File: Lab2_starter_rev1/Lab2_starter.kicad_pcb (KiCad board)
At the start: 4 copper layers, 139.7 x 101.6 mm, 77 parts, among them J1 973582101, J10 Conn_01x02, J11 Conn_01x02, J12 Conn_01x02, J13 Conn_01x02, J14 Conn_01x02, J15 Conn_01x02, J16 Conn_01x02, J2 973582100, J3 973582101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

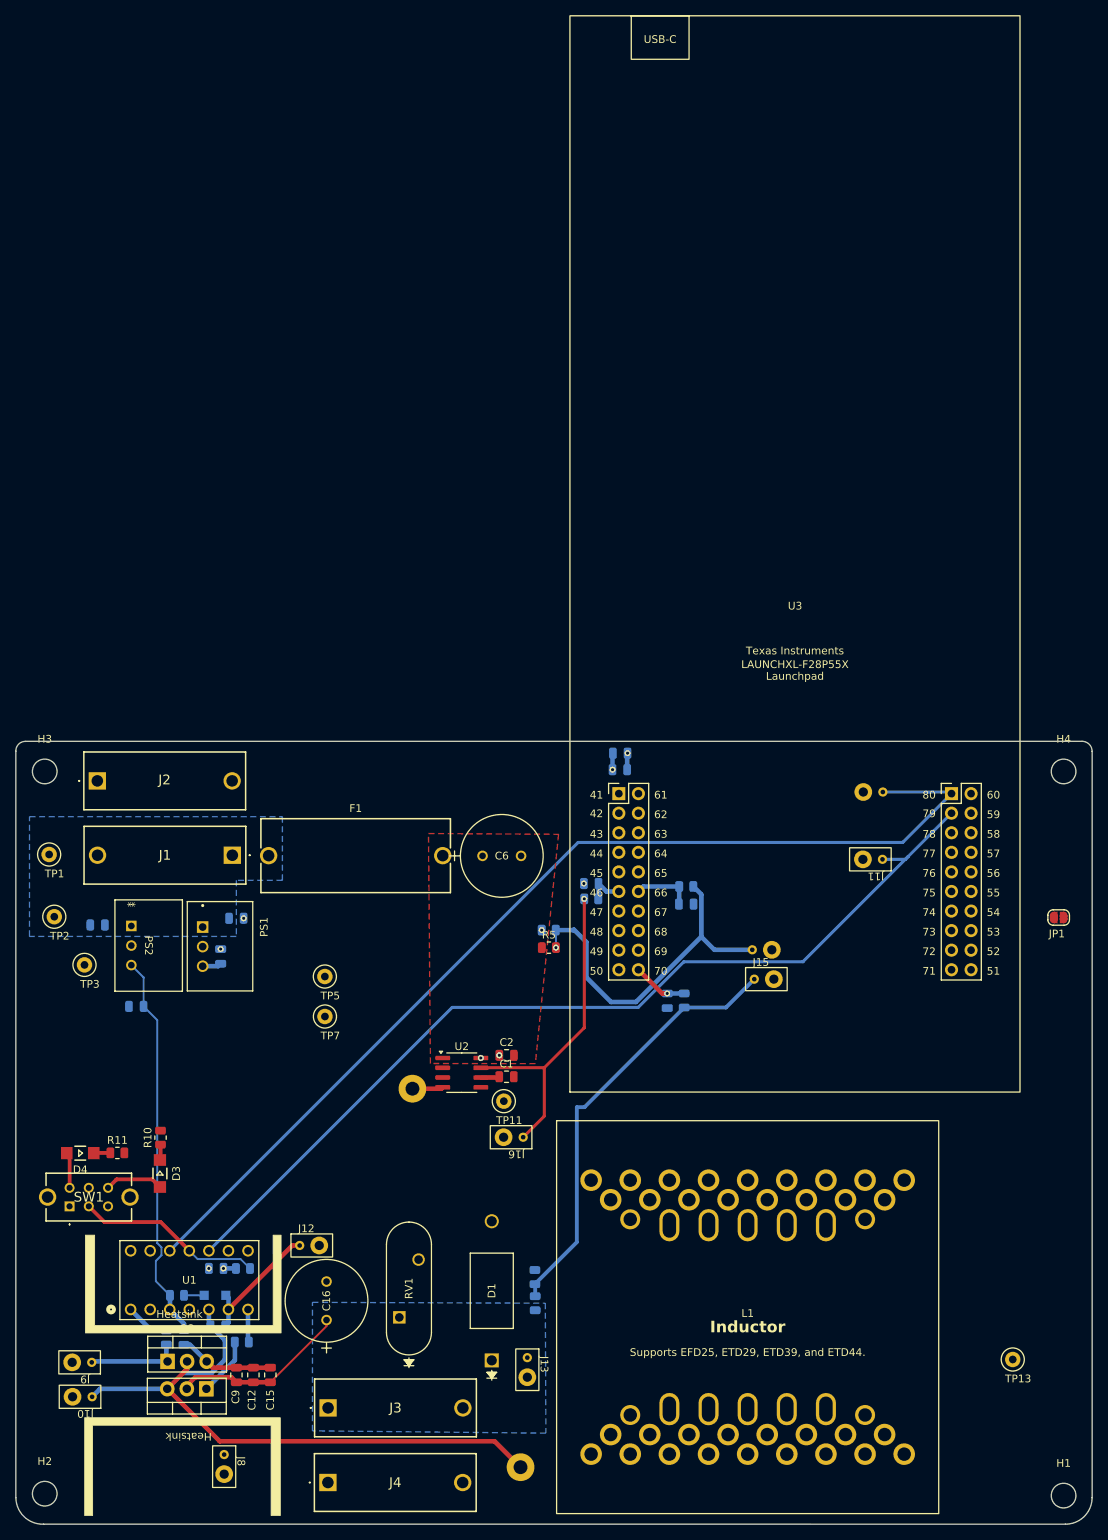
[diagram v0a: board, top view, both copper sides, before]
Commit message: Updated for first PCB upload
Added missing vias to some grounds
Increased width of a few wires
Moved many silkscreens
Added keepout zone for inductor
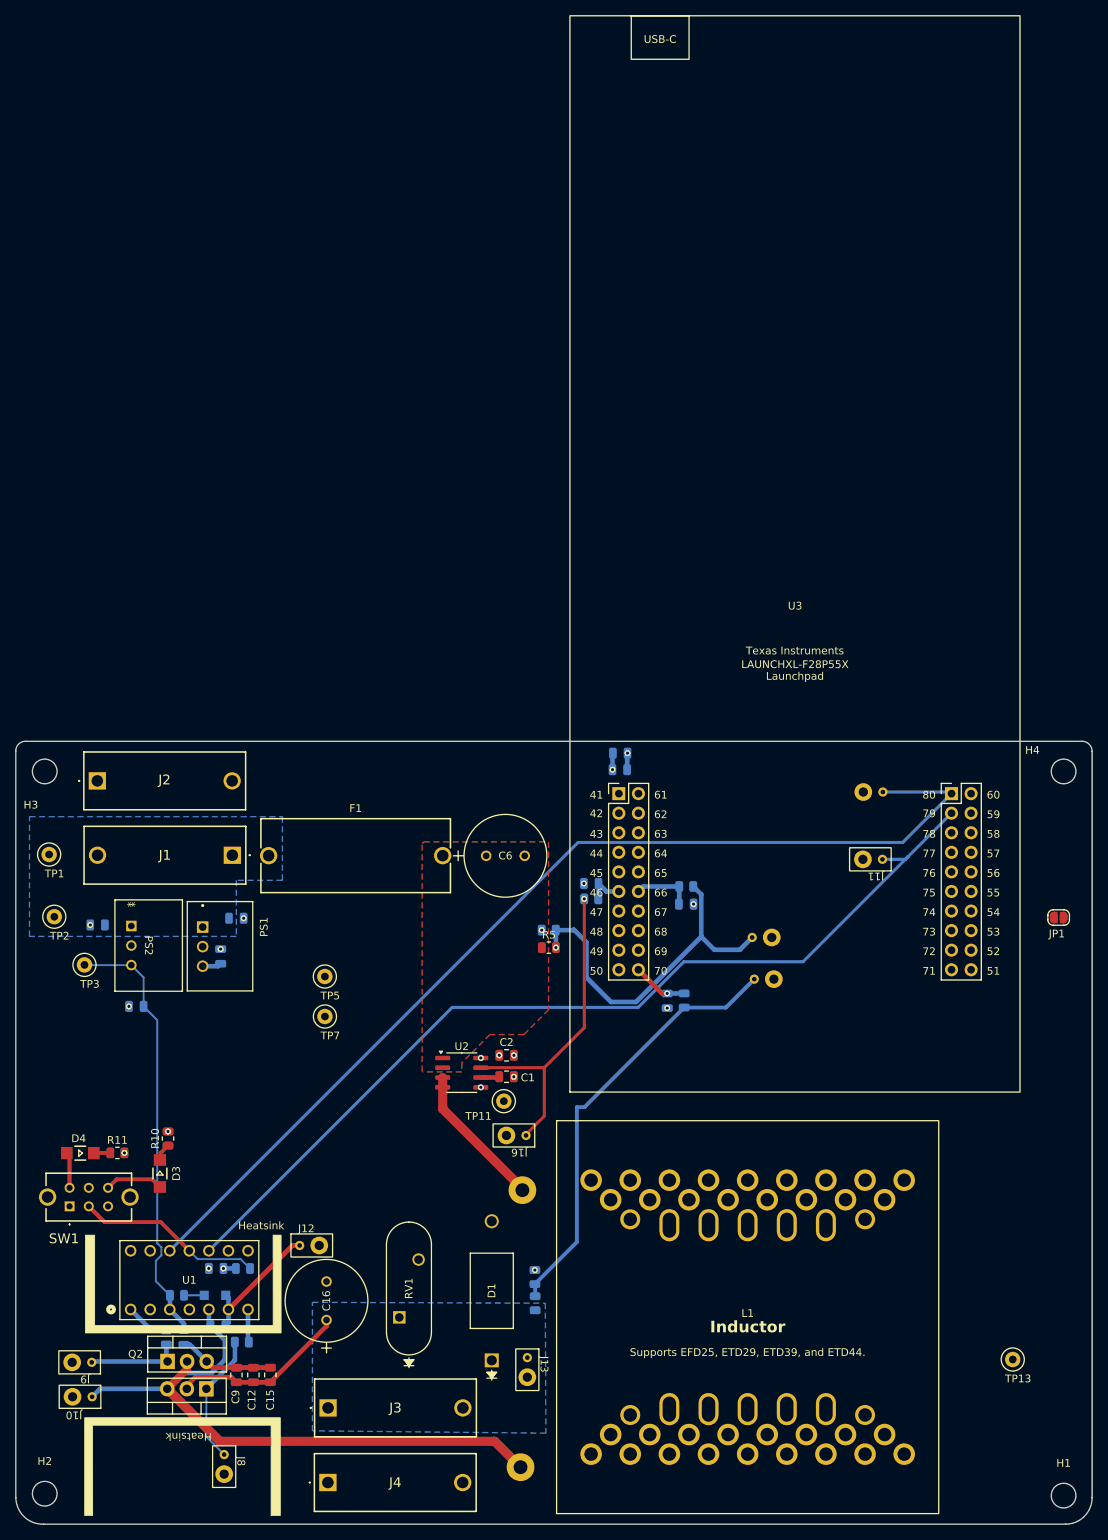
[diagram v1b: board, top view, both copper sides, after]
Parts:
- J15: moved to B.Cu
- moved J6 19.4 mm to (84.5, 97.6)
- moved J14 1.60 mm to (115.6, 64.8)
- moved R10 0.98 mm to (38.5, 90.9)
- moved C6 0.47 mm to (79.8, 54.2)
- moved J16 0.44 mm to (83.7, 90.5)
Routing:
- net Net-(J6-Pin_1): track 4.00 -> 18.9 mm
- net D': track 7.80 -> 17.3 mm
- net +12V: track 51.3 -> 57.4 mm
- net Vin_sens: track 45.5 -> 46.2 mm
- net GND: vias 6 -> 16
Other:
- outline, holes or cut-outs redrawn
